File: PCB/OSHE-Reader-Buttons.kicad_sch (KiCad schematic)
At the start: 0 parts

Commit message: Update OSHE-Reader-Buttons.kicad_sch
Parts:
- added SW1, SW2, SW3, SW4, SW5: SW_Push, symbol Switch:SW_Push

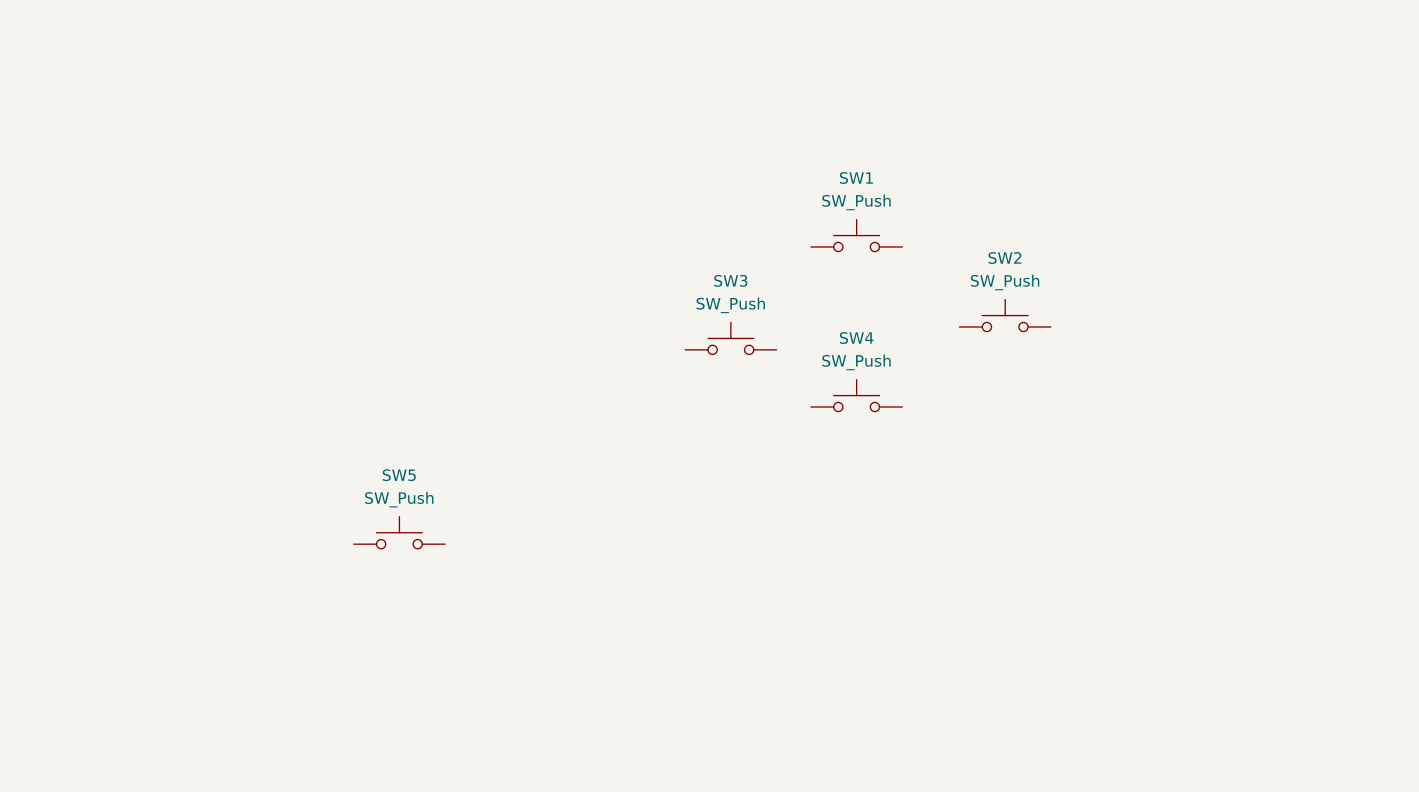
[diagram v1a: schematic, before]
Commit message: Update OSHE-Reader-Buttons.kicad_sch
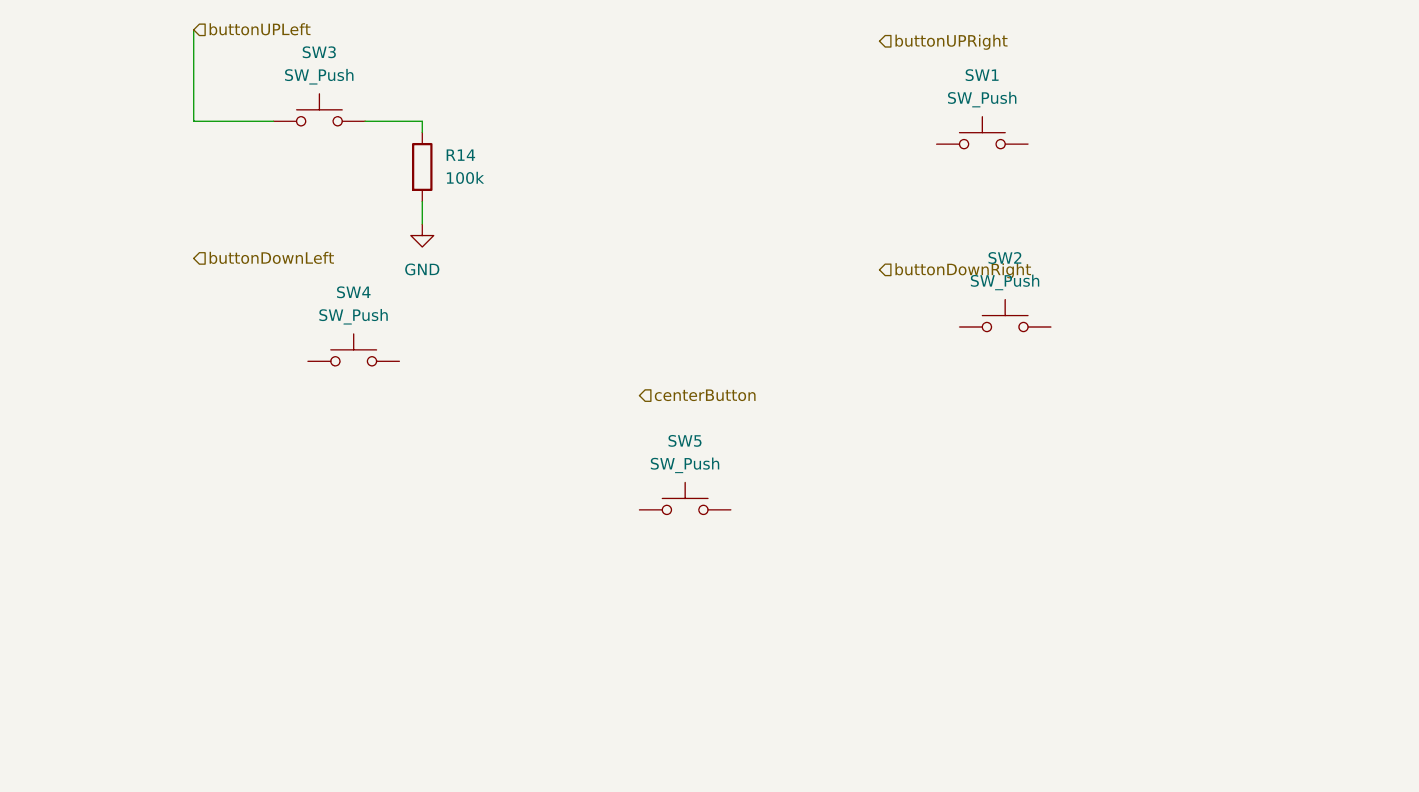
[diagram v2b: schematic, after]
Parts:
- added R14: 100k, symbol Device:R
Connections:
- net buttonUPLeft: now reaches SW3.1
- net at SW3.2: now also R14.1
- new net GND: R14.2
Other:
- moved on the sheet: SW1, SW3, SW4, SW5

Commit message: Update OSHE-Reader-Buttons.kicad_sch
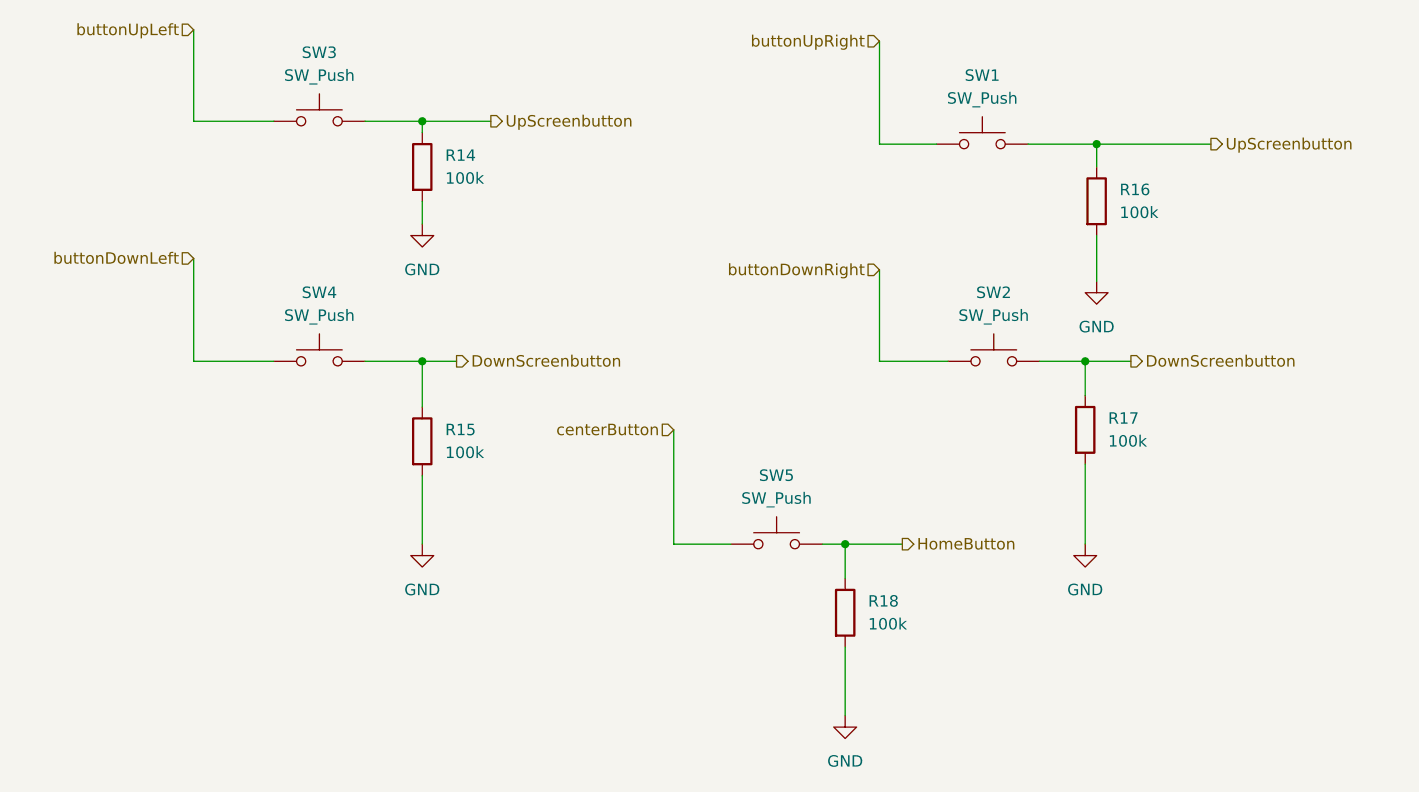
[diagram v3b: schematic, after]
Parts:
- added R15, R16, R17, R18: 100k, symbol Device:R
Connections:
- net GND: now also R15.2, R16.2, R17.2, R18.2
- net buttonDownLeft: now also SW4.1
- net buttonDownRight: now also SW2.1
- net centerButton: now also SW5.1
- net HomeButton: now reaches SW5.2
- net HomeButton: now also R18.1
- net UpScreenbutton: now reaches R14.1, SW3.2
- net UpScreenbutton: now also SW1.2, R16.1
- net DownScreenbutton: now reaches SW2.2
- net DownScreenbutton: now also SW4.2, R15.1, R17.1
- net buttonUpRight: now reaches SW1.1
- net buttonUPLeft renamed buttonUpLeft
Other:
- moved on the sheet: SW2, SW4, SW5

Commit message: put 3v3 on high side of buttons instead of hierarchical pins
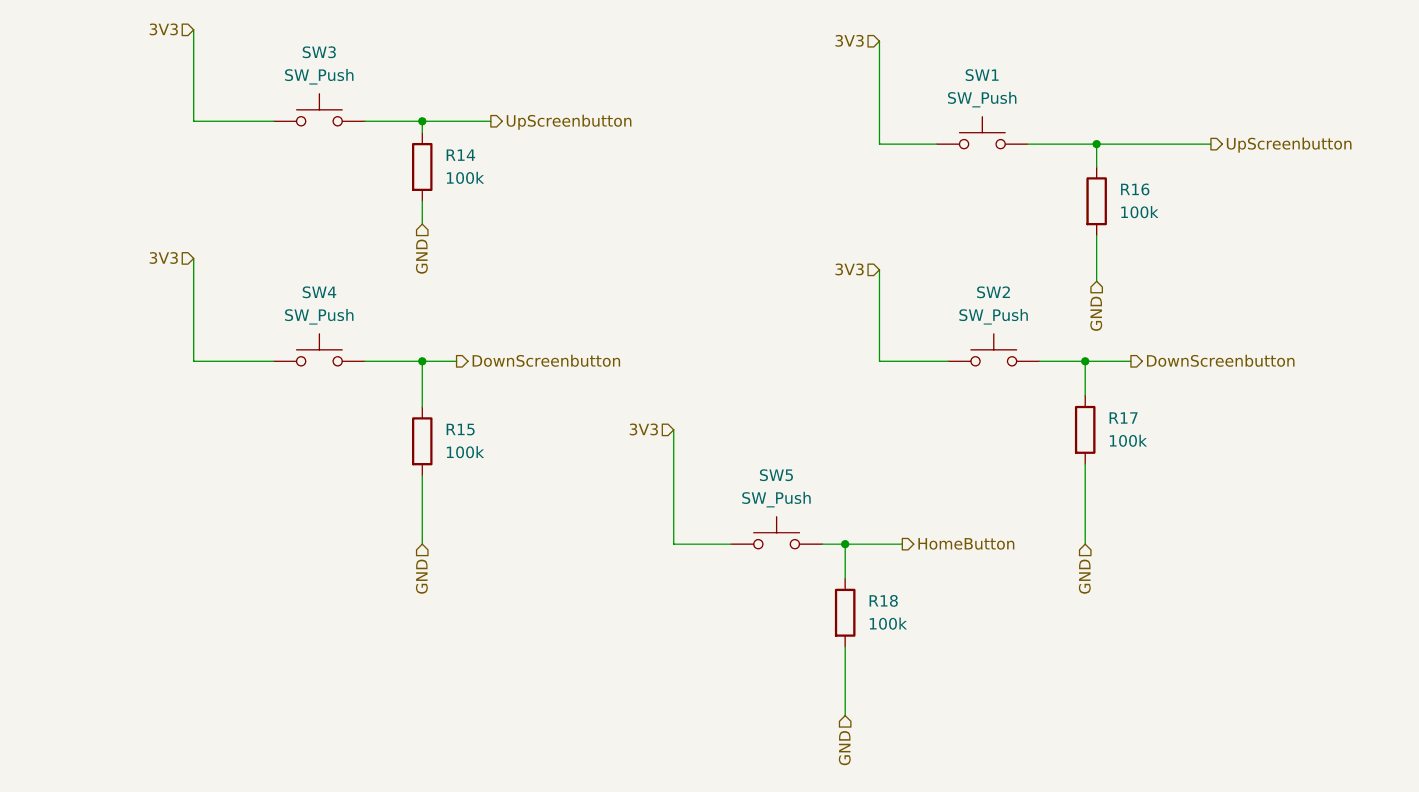
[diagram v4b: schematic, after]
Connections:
- net buttonDownRight is gone; now on net 3V3: SW2.1
- net buttonUpLeft is gone; now on net 3V3: SW3.1
- net buttonUpRight is gone; now on net 3V3: SW1.1
- net centerButton is gone; now on net 3V3: SW5.1
- net buttonDownLeft renamed 3V3

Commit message: hopefully finshed buttons?
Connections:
- net DownScreenbutton: no longer R17.1, SW2.2
- net UpScreenbutton: no longer R16.1, SW1.2
- new net LeftScreenbutton: R16.1, SW1.2
- new net RightScreenbutton: R17.1, SW2.2
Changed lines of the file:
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@@
 		)
 	)
-	(hierarchical_label "UpScreenbutton"
+	(hierarchical_label "LeftScreenbutton"
 		(shape output)
 		(at 153.67 49.53 0)
@@
 		)
 	)
-	(hierarchical_label "DownScreenbutton"
+	(hierarchical_label "RightScreenbutton"
 		(shape output)
 		(at 144.78 73.66 0)

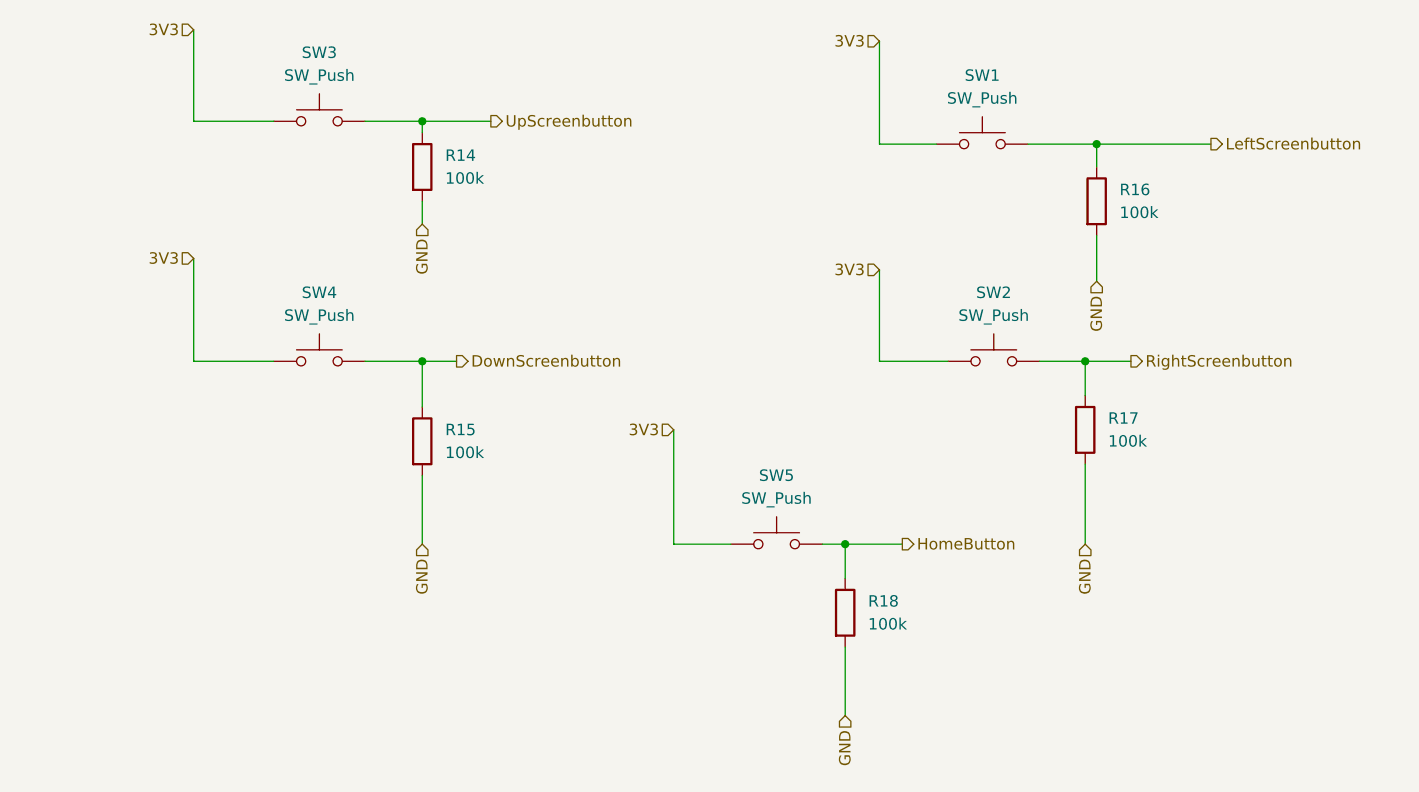
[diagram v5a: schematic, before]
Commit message: Updates reader display connector
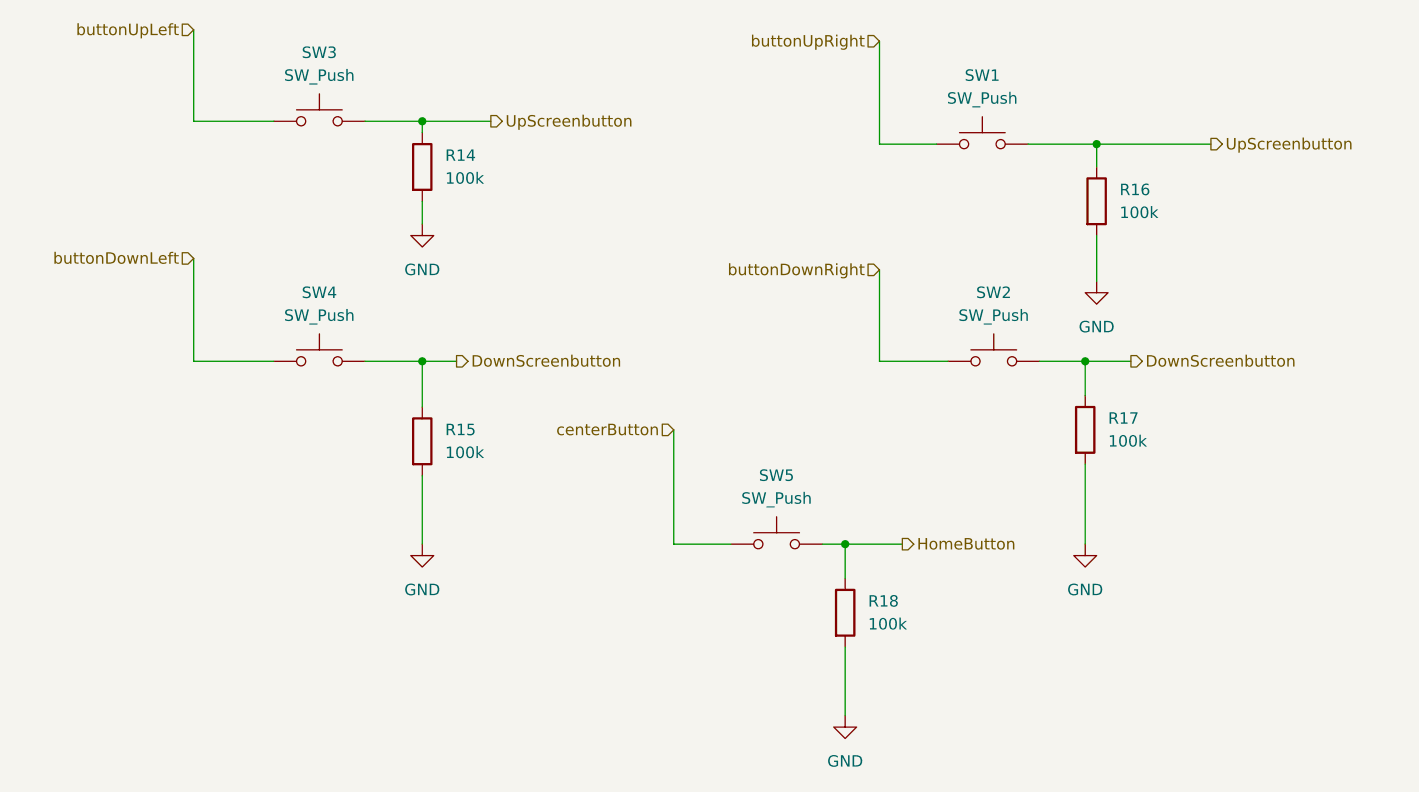
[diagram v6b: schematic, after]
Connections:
- net LeftScreenbutton is gone; now on net UpScreenbutton: R16.1, SW1.2
- net RightScreenbutton is gone; now on net DownScreenbutton: R17.1, SW2.2
- removed net 3V3: SW1.1, SW2.1, SW3.1, SW4.1, SW5.1
- new net buttonDownLeft: SW4.1
- new net buttonDownRight: SW2.1
- new net buttonUpLeft: SW3.1
- new net buttonUpRight: SW1.1
- new net centerButton: SW5.1

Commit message: Updating pins in roots file
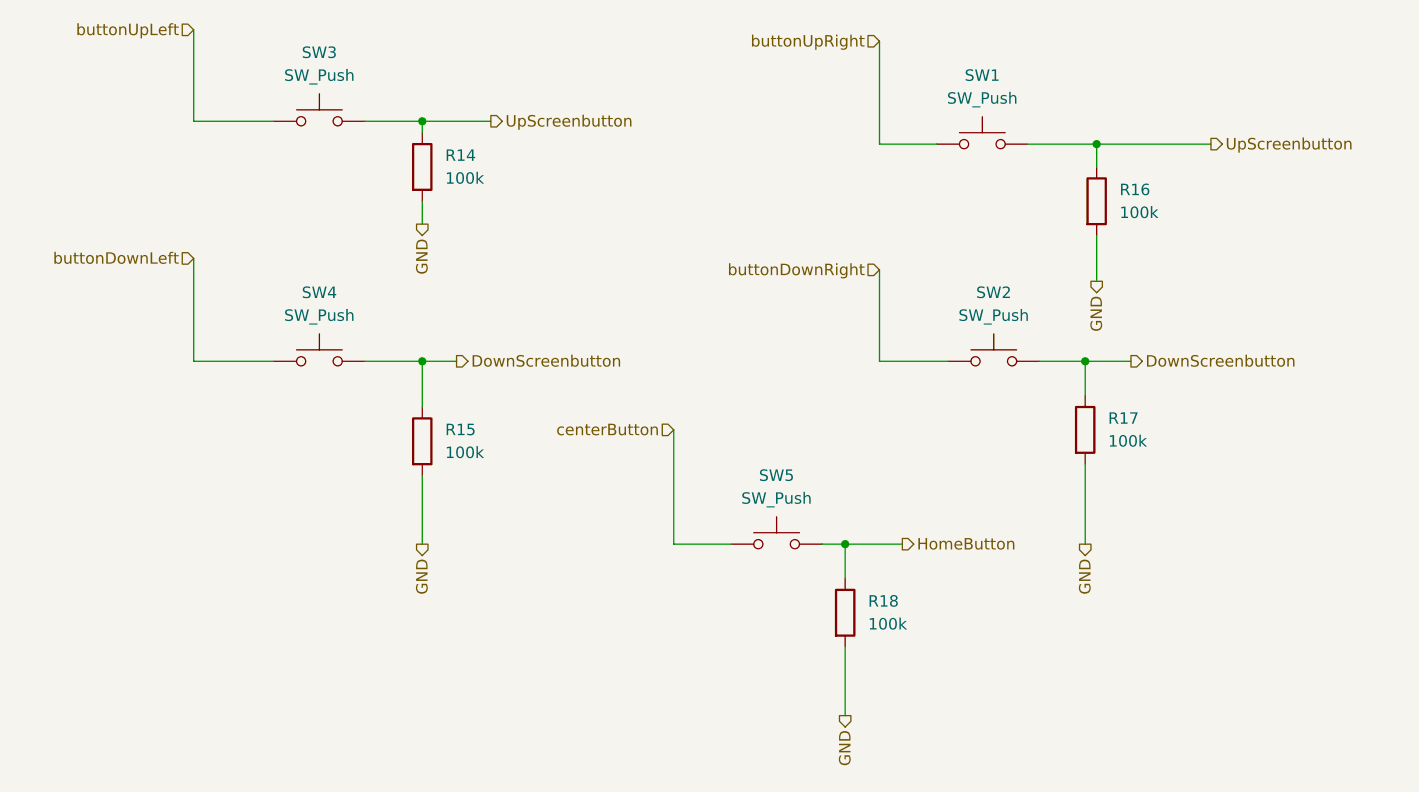
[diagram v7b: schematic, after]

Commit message: HOPEFULLY GOOD FOR EVER (good for first semester) :)
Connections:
- net buttonDownRight is gone; now on net 3V3: SW2.1
- net buttonUpLeft is gone; now on net 3V3: SW3.1
- net buttonUpRight is gone; now on net 3V3: SW1.1
- net centerButton is gone; now on net 3V3: SW5.1
- net DownScreenbutton renamed DownButton
- net DownButton: no longer R17.1, SW2.2
- net UpScreenbutton renamed LeftButton
- net LeftButton: no longer R14.1, SW3.2
- net buttonDownLeft renamed 3V3
- new net RightButton: R17.1, SW2.2
- new net UpButton: R14.1, SW3.2
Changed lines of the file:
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@@
 	)
 	(hierarchical_label "GND"
-		(shape output)
+		(shape input)
 		(at 140.97 64.77 270)
 		(effects
@@
 	)
 	(hierarchical_label "GND"
-		(shape output)
+		(shape input)
 		(at 66.04 93.98 270)
 		(effects
@@
 		)
 	)
-	(hierarchical_label "buttonUpRight"
+	(hierarchical_label "3V3"
 		(shape input)
 		(at 116.84 38.1 180)
@@
 		)
 	)
-	(hierarchical_label "DownScreenbutton"
+	(hierarchical_label "DownButton"
 		(shape output)
 		(at 69.85 73.66 0)
@@
 		)
 	)
-	(hierarchical_label "UpScreenbutton"
+	(hierarchical_label "LeftButton"
 		(shape output)
 		(at 153.67 49.53 0)
@@
 		)
 	)
-	(hierarchical_label "buttonUpLeft"
+	(hierarchical_label "3V3"
 		(shape input)
 		(at 40.64 36.83 180)
@@
 		)
 	)
-	(hierarchical_label "UpScreenbutton"
+	(hierarchical_label "UpButton"
 		(shape output)
 		(at 73.66 46.99 0)
@@
 		)
 	)
-	(hierarchical_label "buttonDownRight"
+	(hierarchical_label "3V3"
 		(shape input)
 		(at 116.84 63.5 180)
@@
 		)
 	)
-	(hierarchical_label "buttonDownLeft"
+	(hierarchical_label "3V3"
 		(shape input)
 		(at 40.64 62.23 180)
@@
 	)
 	(hierarchical_label "GND"
-		(shape output)
+		(shape input)
 		(at 113.03 113.03 270)
 		(effects
@@
 		)
 	)
-	(hierarchical_label "DownScreenbutton"
+	(hierarchical_label "RightButton"
 		(shape output)
 		(at 144.78 73.66 0)
@@
 	)
 	(hierarchical_label "GND"
-		(shape output)
+		(shape input)
 		(at 66.04 58.42 270)
 		(effects
@@
 		)
 	)
-	(hierarchical_label "centerButton"
+	(hierarchical_label "3V3"
 		(shape input)
 		(at 93.98 81.28 180)
@@
 	)
 	(hierarchical_label "GND"
-		(shape output)
+		(shape input)
 		(at 139.7 93.98 270)
 		(effects
